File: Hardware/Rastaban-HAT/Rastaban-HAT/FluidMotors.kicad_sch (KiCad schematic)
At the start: 14 parts, among them U3 TMC2208_Carrier, U4 TMC2208_Carrier

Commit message: enh pcb component layout
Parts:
- C16, C17, C22, C23: Purpose (none) -> decoupling
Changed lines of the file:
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@@
+      (effects (font (size 1.27 1.27)) hide)
+    )
+    (property "Purpose" "decoupling" (id 4) (at 210.185 93.345 0)
       (effects (font (size 1.27 1.27)) hide)
     )
@@
       (effects (font (size 1.27 1.27)) hide)
     )
+    (property "Purpose" "decoupling" (id 6) (at 135.89 100.965 0)
+      (effects (font (size 1.27 1.27)) hide)
+    )
     (pin "1")
     (pin "2")
@@
       (effects (font (size 1.27 1.27)) hide)
     )
+    (property "Purpose" "decoupling" (id 6) (at 216.535 100.965 0)
+      (effects (font (size 1.27 1.27)) hide)
+    )
     (pin "1")
     (pin "2")
@@
       (effects (font (size 1.27 1.27)) hide)
     )
+    (property "Purpose" "decoupling" (id 4) (at 132.08 93.345 0)
+      (effects (font (size 1.27 1.27)) hide)
+    )

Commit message: changed capacitor footprints
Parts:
- C16: footprint Capacitor_THT:C_Radial_D6.3mm_H5.0mm_P2.50mm -> Capacitor_SMD:CP_Elec_8x10
- C17: footprint Capacitor_THT:C_Radial_D6.3mm_H11.0mm_P2.50mm -> Capacitor_SMD:CP_Elec_8x10
- C22, C23: footprint Capacitor_SMD:C_0805_2012Metric_Pad1.18x1.45mm_HandSolder -> Capacitor_SMD:CP_Elec_4x5.4
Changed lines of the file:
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@@
       (effects (font (size 1.27 1.27)) (justify left))
     )
-    (property "Footprint" "Capacitor_SMD:C_0805_2012Metric_Pad1.18x1.45mm_HandSolder" (id 2) (at 211.1502 97.155 0)
+    (property "Footprint" "Capacitor_SMD:CP_Elec_4x5.4" (id 2) (at 211.1502 97.155 0)
       (effects (font (size 1.27 1.27)) hide)
     )
@@
       (effects (font (size 1.27 1.27)) (justify left))
     )
-    (property "Footprint" "Capacitor_THT:C_Radial_D6.3mm_H5.0mm_P2.50mm" (id 2) (at 136.8552 104.775 0)
+    (property "Footprint" "Capacitor_SMD:CP_Elec_8x10" (id 2) (at 136.8552 104.775 0)
       (effects (font (size 1.27 1.27)) hide)
     )
@@
       (effects (font (size 1.27 1.27)) (justify left))
     )
-    (property "Footprint" "Capacitor_THT:C_Radial_D6.3mm_H11.0mm_P2.50mm" (id 2) (at 217.5002 104.775 0)
+    (property "Footprint" "Capacitor_SMD:CP_Elec_8x10" (id 2) (at 217.5002 104.775 0)
       (effects (font (size 1.27 1.27)) hide)
     )
@@
       (effects (font (size 1.27 1.27)) (justify left))
     )
-    (property "Footprint" "Capacitor_SMD:C_0805_2012Metric_Pad1.18x1.45mm_HandSolder" (id 2) (at 133.0452 97.155 0)
-      (effects (font (size 1.27 1.27)) hide)
-    )
+    (property "Footprint" "Capacitor_SMD:CP_Elec_4x5.4" (id 2) (at 133.0452 97.155 0)
+      (effects (font (size 1.27 1.27)) hide)
+    )

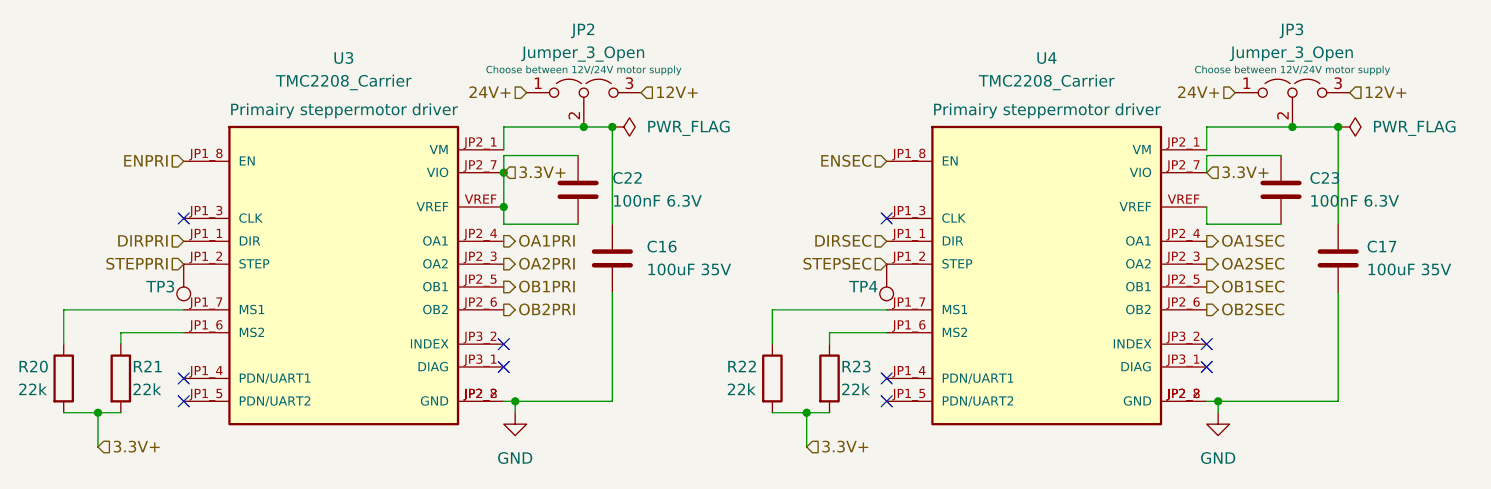
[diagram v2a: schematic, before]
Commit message: added testpoints
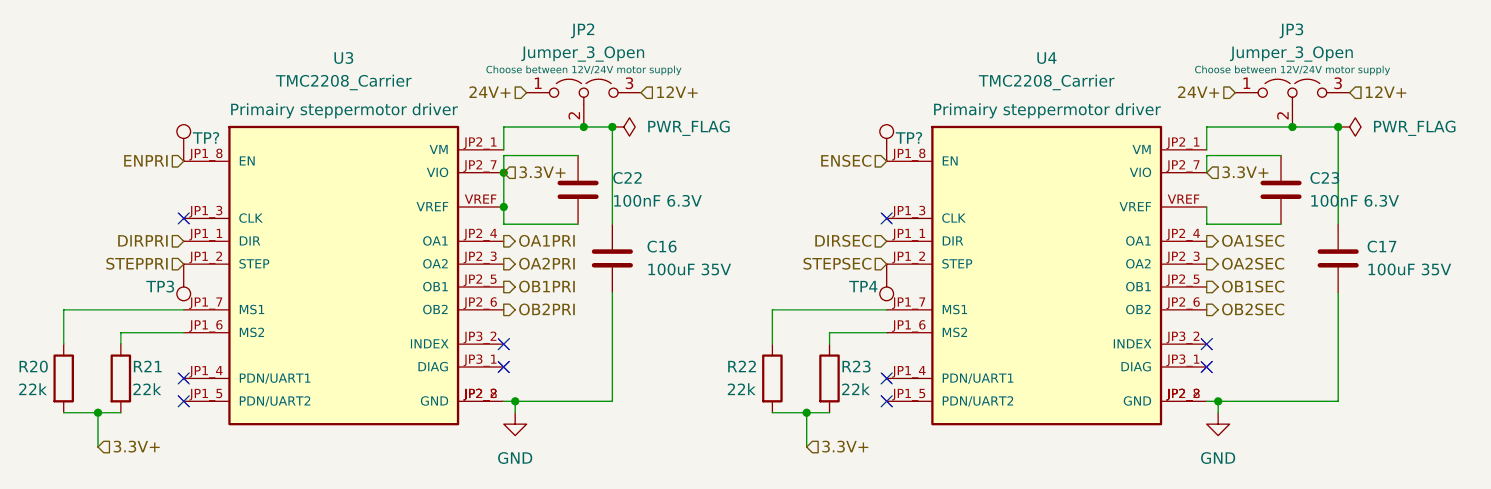
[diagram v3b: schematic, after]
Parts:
- added TP? (x2): TestPoint, TestPoint:TestPoint_THTPad_2.0x2.0mm_Drill1.0mm, symbol Connector:TestPoint
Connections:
- net ENPRI: now also TP?.1
- net ENSEC: now also TP?.1
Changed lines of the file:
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@@
+    (pin "1")
+  )
+  (symbol (lib_id "Connector:TestPoint") (at 88.265 90.17 0) (unit 1)
+    (in_bom yes) (on_board yes)
+    (property "Reference" "TP?" (id 0) (at 90.805 87.63 0))
+    (property "Value" "TestPoint" (id 1) (at 88.265 85.09 0)
+      (effects (font (size 1.27 1.27)) hide)
+    )
+    (property "Footprint" "TestPoint:TestPoint_THTPad_2.0x2.0mm_Drill1.0mm" (id 2) (at 93.345 90.17 0)
+      (effects (font (size 1.27 1.27)) hide)
+    )
+    (property "Datasheet" "~" (id 3) (at 93.345 90.17 0)
+      (effects (font (size 1.27 1.27)) hide)
+    )
     (pin "1")
   )
@@
     (pin "2")
   )
+  (symbol (lib_id "Connector:TestPoint") (at 166.37 90.17 0) (unit 1)
+    (in_bom yes) (on_board yes)
+    (property "Reference" "TP?" (id 0) (at 168.91 87.63 0))
+    (property "Value" "TestPoint" (id 1) (at 166.37 85.09 0)
+      (effects (font (size 1.27 1.27)) hide)
+    )
+    (property "Footprint" "TestPoint:TestPoint_THTPad_2.0x2.0mm_Drill1.0mm" (id 2) (at 171.45 90.17 0)
+      (effects (font (size 1.27 1.27)) hide)
+    )
+    (property "Datasheet" "~" (id 3) (at 171.45 90.17 0)
+      (effects (font (size 1.27 1.27)) hide)
+    )
+    (pin "1")
+  )
   (symbol (lib_id "Device:C") (at 216.535 100.965 0) (unit 1)

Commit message: Removed LEDS
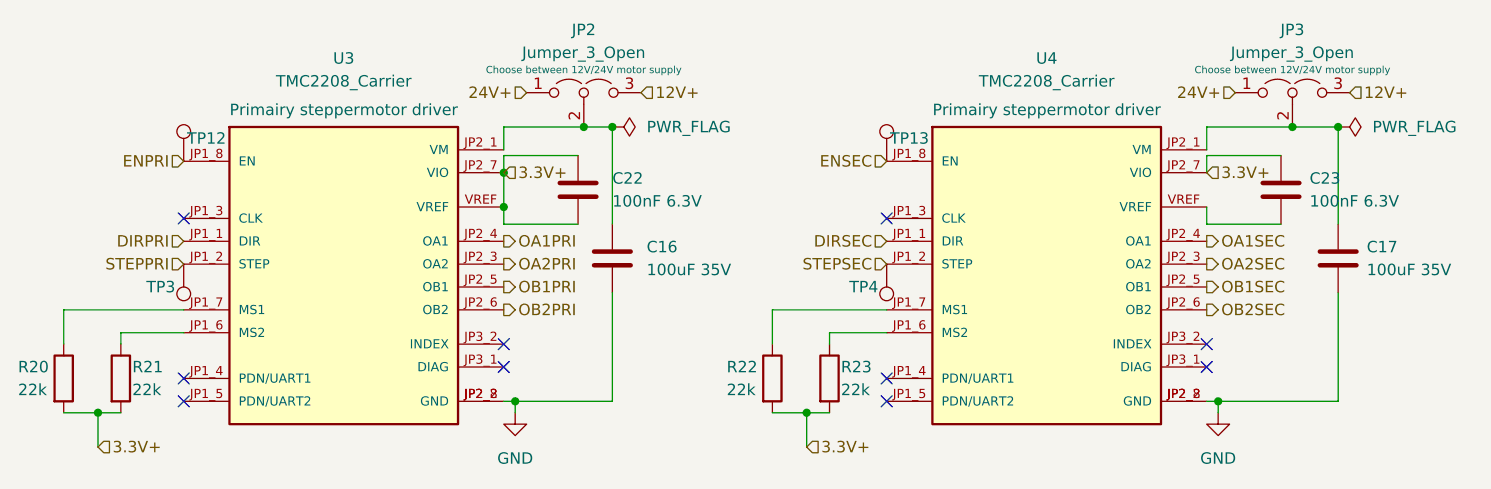
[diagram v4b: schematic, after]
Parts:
- gave numbers to parts that had none: 2
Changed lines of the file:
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@@
   (symbol (lib_id "Connector:TestPoint") (at 88.265 90.17 0) (unit 1)
     (in_bom yes) (on_board yes)
-    (property "Reference" "TP?" (id 0) (at 90.805 87.63 0))
+    (property "Reference" "TP12" (id 0) (at 90.805 87.63 0))
     (property "Value" "TestPoint" (id 1) (at 88.265 85.09 0)
       (effects (font (size 1.27 1.27)) hide)
@@
   (symbol (lib_id "Connector:TestPoint") (at 166.37 90.17 0) (unit 1)
     (in_bom yes) (on_board yes)
-    (property "Reference" "TP?" (id 0) (at 168.91 87.63 0))
+    (property "Reference" "TP13" (id 0) (at 168.91 87.63 0))
     (property "Value" "TestPoint" (id 1) (at 166.37 85.09 0)
       (effects (font (size 1.27 1.27)) hide)

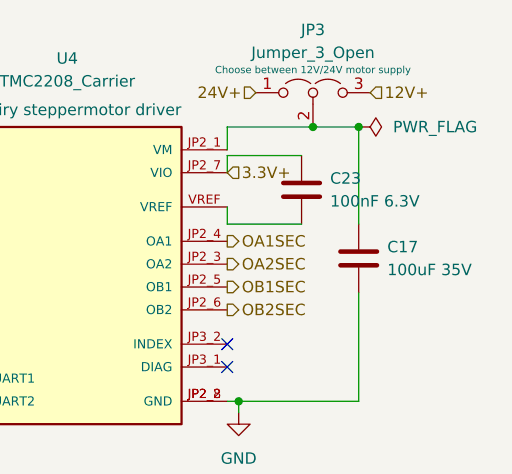
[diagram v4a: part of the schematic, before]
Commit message: Started changing capacitor types and sizes
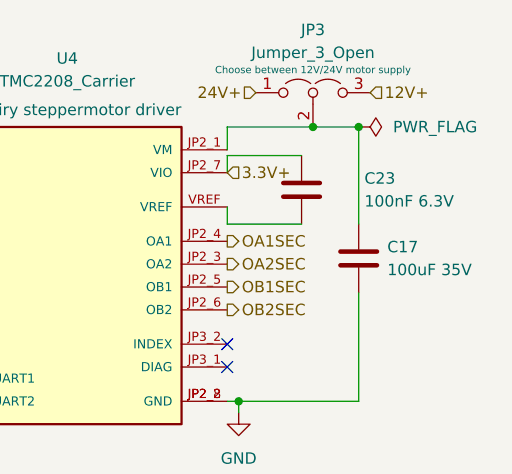
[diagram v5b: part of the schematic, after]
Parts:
- C22, C23: footprint Capacitor_SMD:CP_Elec_4x5.4 -> Capacitor_SMD:C_0805_2012Metric_Pad1.18x1.45mm_HandSolder
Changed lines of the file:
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@@
   )
   (symbol (lib_id "Device:C") (at 210.185 93.345 0) (unit 1)
-    (in_bom yes) (on_board yes) (fields_autoplaced)
-    (property "Reference" "C23" (id 0) (at 213.36 92.0749 0)
-      (effects (font (size 1.27 1.27)) (justify left))
-    )
-    (property "Value" "100nF 6.3V" (id 1) (at 213.36 94.6149 0)
-      (effects (font (size 1.27 1.27)) (justify left))
-    )
-    (property "Footprint" "Capacitor_SMD:CP_Elec_4x5.4" (id 2) (at 211.1502 97.155 0)
+    (in_bom yes) (on_board yes)
+    (property "Reference" "C23" (id 0) (at 217.17 92.075 0)
+      (effects (font (size 1.27 1.27)) (justify left))
+    )
+    (property "Value" "100nF 6.3V" (id 1) (at 217.17 94.615 0)
+      (effects (font (size 1.27 1.27)) (justify left))
+    )
+    (property "Footprint" "Capacitor_SMD:C_0805_2012Metric_Pad1.18x1.45mm_HandSolder" (id 2) (at 211.1502 97.155 0)
       (effects (font (size 1.27 1.27)) hide)
     )
@@
       (effects (font (size 1.27 1.27)) (justify left))
     )
-    (property "Footprint" "Capacitor_SMD:CP_Elec_4x5.4" (id 2) (at 133.0452 97.155 0)
-      (effects (font (size 1.27 1.27)) hide)
-    )
+    (property "Footprint" "Capacitor_SMD:C_0805_2012Metric_Pad1.18x1.45mm_HandSolder" (id 2) (at 133.0452 97.155 0)
+      (effects (font (size 1.27 1.27)) hide)
+    )

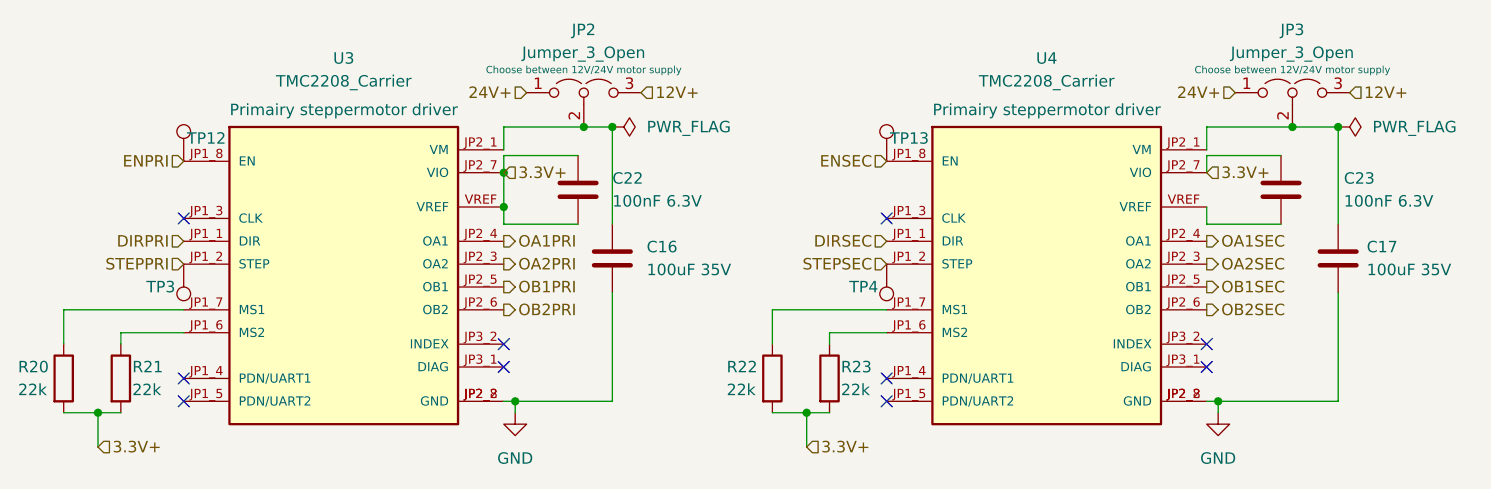
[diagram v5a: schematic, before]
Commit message: changed all capacitor voltages to 50V
This makes ordering and component selection easier.
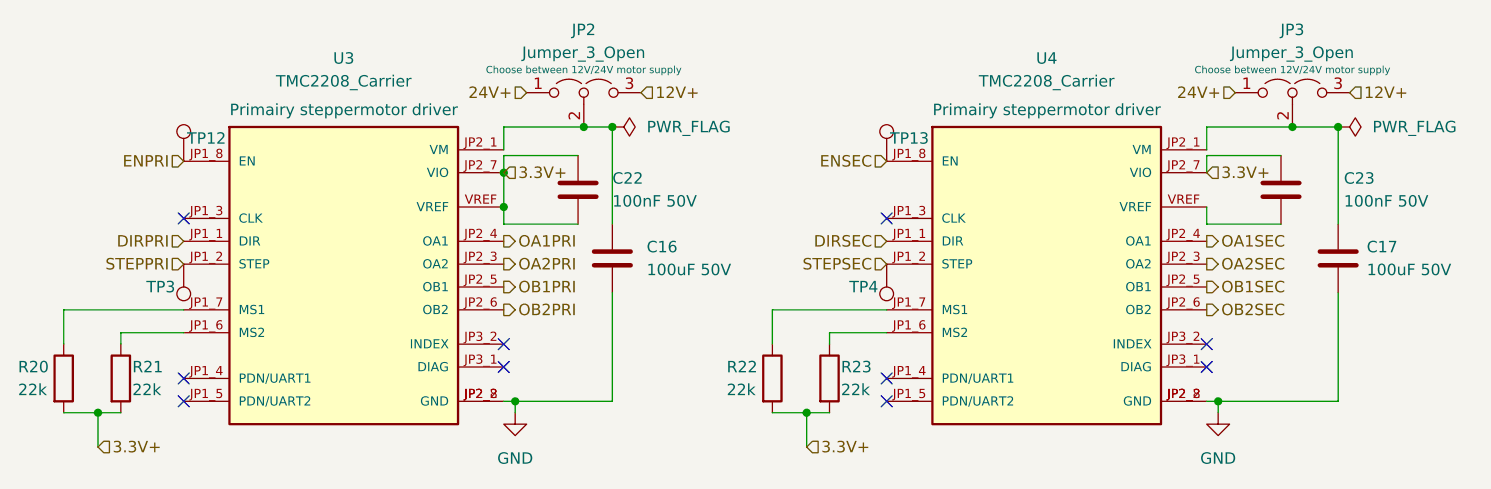
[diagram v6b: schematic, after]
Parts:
- C16, C17: value 100uF 35V -> 100uF 50V
- C22, C23: value 100nF 6.3V -> 100nF 50V
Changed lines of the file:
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@@
       (effects (font (size 1.27 1.27)) (justify left))
     )
-    (property "Value" "100nF 6.3V" (id 1) (at 217.17 94.615 0)
+    (property "Value" "100nF 50V" (id 1) (at 217.17 94.615 0)
       (effects (font (size 1.27 1.27)) (justify left))
     )
@@
       (effects (font (size 1.27 1.27)) (justify left))
     )
-    (property "Value" "100uF 35V" (id 1) (at 139.7 102.2349 0)
+    (property "Value" "100uF 50V" (id 1) (at 139.7 102.2349 0)
       (effects (font (size 1.27 1.27)) (justify left))
     )
@@
       (effects (font (size 1.27 1.27)) (justify left))
     )
-    (property "Value" "100uF 35V" (id 1) (at 219.71 102.2349 0)
+    (property "Value" "100uF 50V" (id 1) (at 219.71 102.2349 0)
       (effects (font (size 1.27 1.27)) (justify left))
     )
@@
       (effects (font (size 1.27 1.27)) (justify left))
     )
-    (property "Value" "100nF 6.3V" (id 1) (at 135.89 94.6149 0)
-      (effects (font (size 1.27 1.27)) (justify left))
-    )
+    (property "Value" "100nF 50V" (id 1) (at 135.89 94.6149 0)
+      (effects (font (size 1.27 1.27)) (justify left))
+    )

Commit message: finished BOM file
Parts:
- C16, C17: LCSC (none) -> C445063
- C22, C23: LCSC (none) -> C531179
- JP2, JP3, TP12, TP13, TP3, TP4: LCSC (none) -> x; Mouser (none) -> x
- R20, R21, R22, R23: LCSC (none) -> C114565
- U3, U4: TinyTronics (none) -> https://www.tinytronics.nl/shop/nl/mechanica-en-actuatoren/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
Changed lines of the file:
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@@
+      (effects (font (size 1.27 1.27)) hide)
+    )
+    (property "LCSC" "x" (id 4) (at 166.37 101.6 0)
+      (effects (font (size 1.27 1.27)) hide)
+    )
+    (property "Mouser" "x" (id 5) (at 166.37 101.6 0)
       (effects (font (size 1.27 1.27)) hide)
     )
@@
       (effects (font (size 0.8 0.8)))
     )
+    (property "LCSC" "x" (id 5) (at 132.715 82.55 0)
+      (effects (font (size 1.27 1.27)) hide)
+    )
+    (property "Mouser" "x" (id 6) (at 132.715 82.55 0)
+      (effects (font (size 1.27 1.27)) hide)
+    )
     (pin "1")
     (pin "2")
@@
     )
     (property "Datasheet" "~" (id 3) (at 153.67 114.3 0)
+      (effects (font (size 1.27 1.27)) hide)
+    )
+    (property "LCSC" "C114565" (id 4) (at 153.67 114.3 0)
       (effects (font (size 1.27 1.27)) hide)
     )
@@
       (effects (font (size 0.8 0.8)))
     )
+    (property "LCSC" "x" (id 5) (at 211.455 82.55 0)
+      (effects (font (size 1.27 1.27)) hide)
+    )
+    (property "Mouser" "x" (id 6) (at 211.455 82.55 0)
+      (effects (font (size 1.27 1.27)) hide)
+    )
     (pin "1")
     (pin "2")
@@
       (effects (font (size 1.27 1.27)) hide)
     )
+    (property "LCSC" "C531179" (id 5) (at 210.185 93.345 0)
+      (effects (font (size 1.27 1.27)) hide)
+    )
     (pin "1")
     (pin "2")
@@
     )
     (property "Datasheet" "~" (id 3) (at 81.28 114.3 0)
+      (effects (font (size 1.27 1.27)) hide)
+    )
+    (property "LCSC" "C114565" (id 4) (at 81.28 114.3 0)
       (effects (font (size 1.27 1.27)) hide)
     )
@@
     )
     (property "Datasheet" "~" (id 3) (at 93.345 90.17 0)
+      (effects (font (size 1.27 1.27)) hide)
+    )
+    (property "LCSC" "x" (id 4) (at 88.265 90.17 0)
+      (effects (font (size 1.27 1.27)) hide)
+    )
+    (property "Mouser" "x" (id 5) (at 88.265 90.17 0)
       (effects (font (size 1.27 1.27)) hide)
     )
@@
     )
     (property "Purpose" "Primairy steppermotor driver" (id 5) (at 184.15 84.455 0))
+    (property "TinyTronics" "https://www.tinytronics.nl/shop/nl/mechanica-en-actuatoren/motoraansturingen-en-drivers/stappen-motoraansturingen-en-drivers/tmc2208-motor-driver-module" (id 6) (at 184.15 104.14 0)
+      (effects (font (size 1.27 1.27)) hide)
+    )
     (pin "JP1_1")
     (pin "JP1_2")
@@
       (effects (font (size 1.27 1.27)) hide)
     )
+    (property "LCSC" "C114565" (id 4) (at 160.02 114.3 0)
+      (effects (font (size 1.27 1.27)) hide)
+    )
     (pin "1")
     (pin "2")
@@
     )
     (property "Purpose" "decoupling" (id 6) (at 135.89 100.965 0)
+      (effects (font (size 1.27 1.27)) hide)
+    )
+    (property "LCSC" "C445063" (id 7) (at 135.89 100.965 0)
       (effects (font (size 1.27 1.27)) hide)
     )
@@
     )
     (property "Purpose" "Primairy steppermotor driver" (id 5) (at 106.045 84.455 0))
+    (property "TinyTronics" "https://www.tinytronics.nl/shop/nl/mechanica-en-actuatoren/motoraansturingen-en-drivers/stappen-motoraansturingen-en-drivers/tmc2208-motor-driver-module" (id 6) (at 106.045 104.14 0)
+      (effects (font (size 1.27 1.27)) hide)
+    )
     (pin "JP1_1")
     (pin "JP1_2")
@@
       (effects (font (size 1.27 1.27)) hide)
     )
+    (property "LCSC" "C114565" (id 4) (at 74.93 114.3 0)
+      (effects (font (size 1.27 1.27)) hide)
+    )
     (pin "1")
     (pin "2")
@@
       (effects (font (size 1.27 1.27)) hide)
     )
+    (property "LCSC" "x" (id 4) (at 166.37 90.17 0)
+      (effects (font (size 1.27 1.27)) hide)
+    )
+    (property "Mouser" "x" (id 5) (at 166.37 90.17 0)
+      (effects (font (size 1.27 1.27)) hide)
+    )
     (pin "1")
   )
@@
     )
     (property "Purpose" "decoupling" (id 6) (at 216.535 100.965 0)
+      (effects (font (size 1.27 1.27)) hide)
+    )
+    (property "LCSC" "C445063" (id 7) (at 216.535 100.965 0)
       (effects (font (size 1.27 1.27)) hide)
     )
@@
       (effects (font (size 1.27 1.27)) hide)
     )
+    (property "LCSC" "x" (id 4) (at 88.265 101.6 0)
+      (effects (font (size 1.27 1.27)) hide)
+    )
+    (property "Mouser" "x" (id 5) (at 88.265 101.6 0)
+      (effects (font (size 1.27 1.27)) hide)
+    )
     (pin "1")
   )
@@
       (effects (font (size 1.27 1.27)) hide)
     )
+    (property "LCSC" "C531179" (id 5) (at 132.08 93.345 0)
+      (effects (font (size 1.27 1.27)) hide)
+    )

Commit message: continued programming course
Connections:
- net 3.3V+: no longer C22.2, U3.VREF
- new net: C22.2, U3.VREF
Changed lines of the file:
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@@
   (junction (at 211.455 86.36) (diameter 0) (color 0 0 0 0)
   )
-  (junction (at 123.825 91.44) (diameter 0) (color 0 0 0 0)
-  )
   (junction (at 203.2 116.84) (diameter 0) (color 0 0 0 0)
-  )
-  (junction (at 123.825 95.25) (diameter 0) (color 0 0 0 0)
   )
   (junction (at 125.095 116.84) (diameter 0) (color 0 0 0 0)
@@
     (stroke (width 0) (type default) (color 0 0 0 0))
   )
-  (wire (pts (xy 123.825 91.44) (xy 123.825 95.25))
-    (stroke (width 0) (type default) (color 0 0 0 0))
-  )
